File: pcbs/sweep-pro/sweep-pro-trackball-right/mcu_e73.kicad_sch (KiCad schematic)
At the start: 33 parts, among them J11 Conn_01x04_Female, J12 USB-C USB 2.0 MC-372, Q1 AO3407, Q2 AO3407, U1 E73-2G4M08S1C, U2 SRV05-4, U3 XC6220B331MR-G, U4 MAX17048, U5 TP4054, X1 32.768 kHz

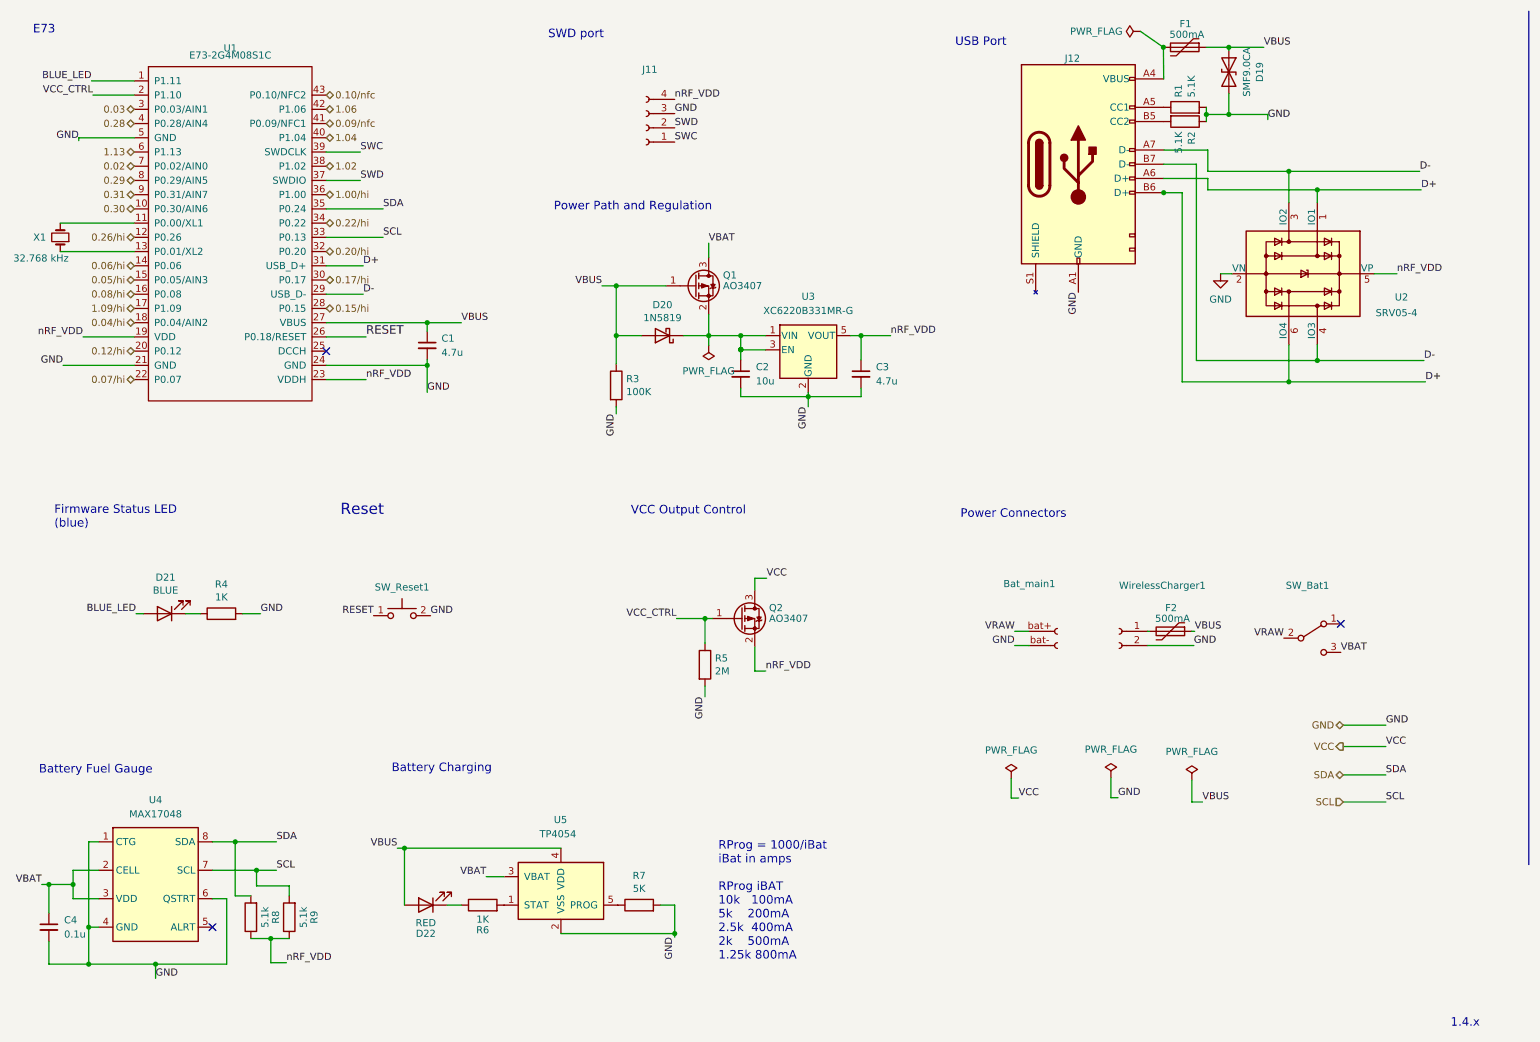
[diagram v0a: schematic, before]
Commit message: init version with integrated trackball in thumb position
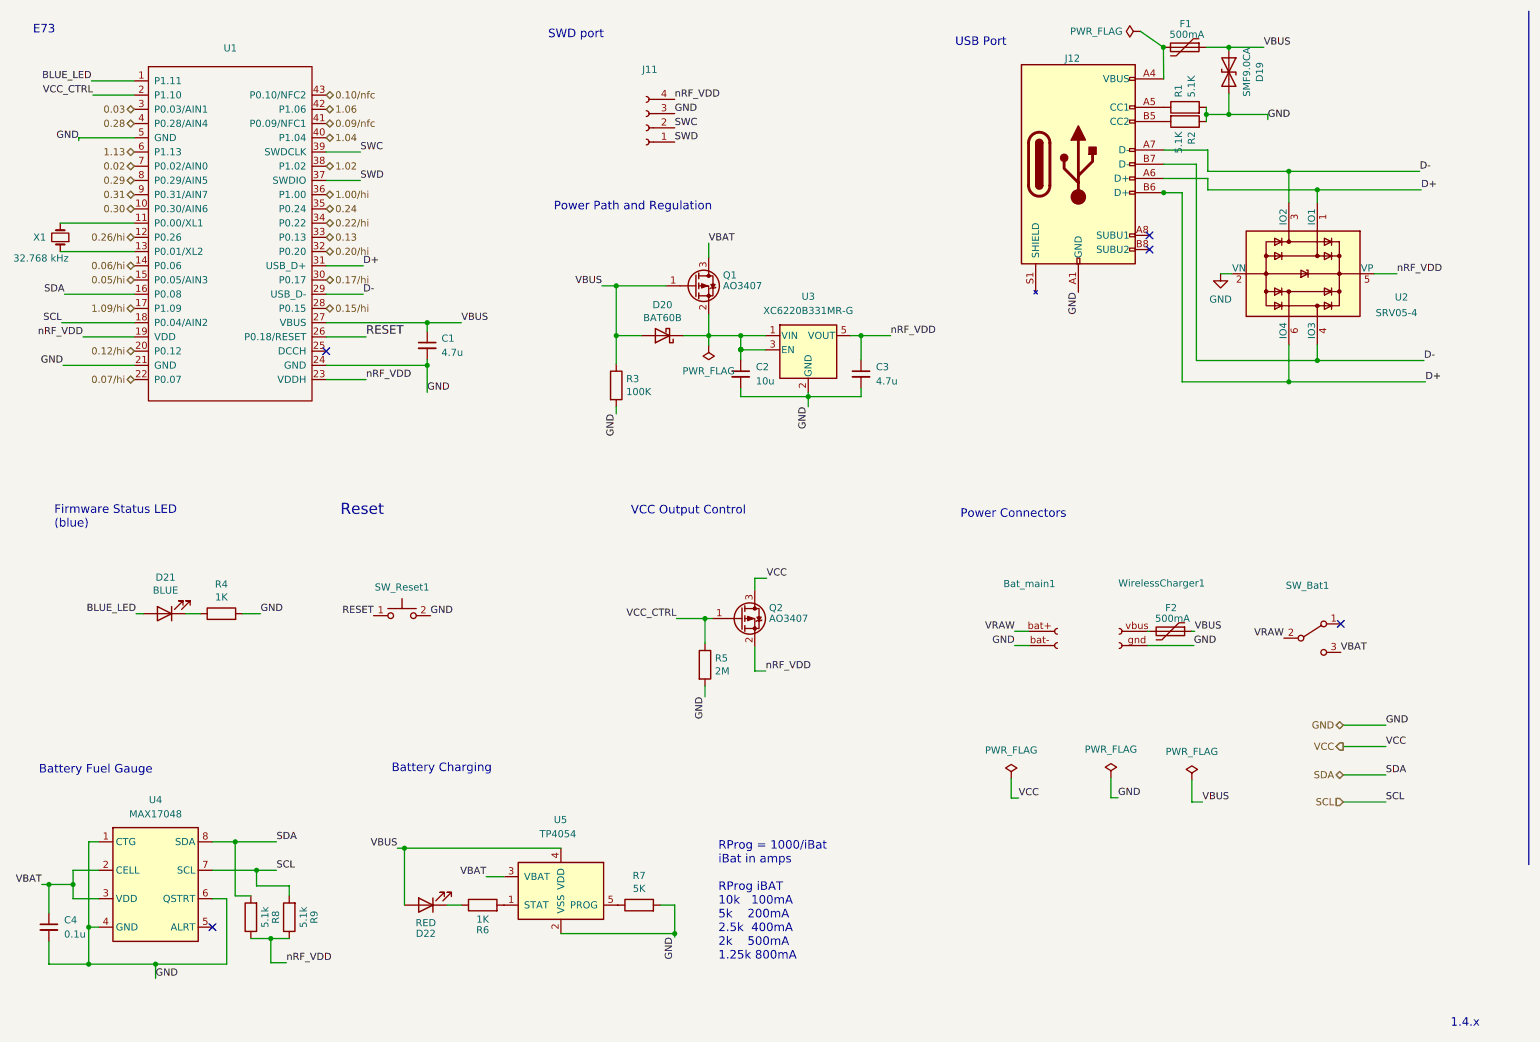
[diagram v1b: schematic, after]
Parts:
- D19: footprint Diode_SMD:D_SOD-123 -> Diode_SMD:D_SOD-123F
- D20: value 1N5819 -> BAT60B; footprint Diode_SMD:D_SOD-323F -> Diode_SMD:D_SOD-323
- J11: footprint (none) -> Connector_PinHeader_2.54mm:PinHeader_1x04_P2.54mm_Vertical
- U1: footprint nrfmicro:E73-2G4M08S1C-52840 -> mylib:E73-2G4M08S1C-52840
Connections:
- net 0.04/hi is gone; now on net SCL: U1.18 (P0.04/AIN2)
- net 0.08/hi is gone; now on net SDA: U1.16 (P0.08)
- net GND: now also WirelessCharger1.gnd; no longer WirelessCharger1.2 (Pin_2)
- net SCL: no longer U1.33 (P0.13)
- net SDA: no longer U1.35 (P0.24)
- net SWC: now also J11.2 (Pin_2); no longer J11.1 (Pin_1)
- net SWD: now also J11.1 (Pin_1); no longer J11.2 (Pin_2)
- net at F2.2: now also WirelessCharger1.vbus; no longer WirelessCharger1.1 (Pin_1)
- new net 0.13: U1.33 (P0.13)
- new net 0.24: U1.35 (P0.24)
- no-connect marks 3 -> 5
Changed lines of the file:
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@@
   (no_connect (at 250.7742 124.4092))
   (no_connect (at 69.596 75.692))
+  (no_connect (at 216.6112 55.0164))
+  (no_connect (at 216.6112 57.5564))
   (wire (pts (xy 191.9224 152.0444) (xy 191.9224 155.4988))
     (stroke (width 0) (type default) (color 0 0 0 0))
@@
     (stroke (width 0) (type default) (color 0 0 0 0))
   )
+  (wire (pts (xy 22.86 65.532) (xy 35.306 65.532))
+    (stroke (width 0) (type default) (color 0 0 0 0))
+  )
   (wire (pts (xy 165.1 83.82) (xy 155.6766 83.82))
     (stroke (width 0) (type default) (color 0 0 0 0))
   )
+  (wire (pts (xy 22.352 70.612) (xy 35.306 70.612))
+    (stroke (width 0) (type default) (color 0 0 0 0))
+  )
   (wire (pts (xy 246.5832 46.8884) (xy 246.5832 49.1744))
     (stroke (width 0) (type default) (color 0 0 0 0))
@@
     (stroke (width 0) (type default) (color 0 0 0 0))
   )
-  (wire (pts (xy 69.596 55.372) (xy 79.756 55.372))
-    (stroke (width 0) (type default) (color 0 0 0 0))
-  )
   (wire (pts (xy 56.134 172.974) (xy 53.34 172.974))
     (stroke (width 0) (type default) (color 0 0 0 0))
@@
   )
   (wire (pts (xy 87.63 78.232) (xy 87.63 77.216))
-    (stroke (width 0) (type default) (color 0 0 0 0))
-  )
-  (wire (pts (xy 69.596 50.292) (xy 79.756 50.292))
     (stroke (width 0) (type default) (color 0 0 0 0))
   )
@@
     (effects (font (size 1.27 1.27)) (justify left bottom))
   )
-  (label "GND" (at 88.2142 122.936 0)
-    (effects (font (size 1.27 1.27)) (justify left bottom))
+  (label "RESET" (at 78.0542 122.936 180)
+    (effects (font (size 1.27 1.27)) (justify right bottom))
   )
   (label "GND" (at 39.116 187.706 0)
@@
     (effects (font (size 1.27 1.27)) (justify right bottom))
   )
-  (label "SCL" (at 79.756 55.372 0)
-    (effects (font (size 1.27 1.27)) (justify left bottom))
-  )
   (label "GND" (at 87.63 83.058 0)
     (effects (font (size 1.27 1.27)) (justify left bottom))
+  )
+  (label "SCL" (at 22.352 70.612 180)
+    (effects (font (size 1.27 1.27)) (justify right bottom))
   )
   (label "D-" (at 265.6332 77.3684 0)
@@
     (effects (font (size 1.27 1.27)) (justify right bottom))
   )
-  (label "SWD" (at 131.826 35.814 0)
+  (label "SWC" (at 131.826 35.814 0)
     (effects (font (size 1.27 1.27)) (justify left bottom))
   )
@@
     (effects (font (size 1.27 1.27)) (justify left bottom))
   )
-  (label "RESET" (at 78.0542 122.936 180)
-    (effects (font (size 1.27 1.27)) (justify right bottom))
+  (label "SDA" (at 22.86 65.532 180)
+    (effects (font (size 1.27 1.27)) (justify right bottom))
+  )
+  (label "GND" (at 88.2142 122.936 0)
+    (effects (font (size 1.27 1.27)) (justify left bottom))
   )
   (label "nRF_VDD" (at 170.3832 72.9234 0)
@@
     (effects (font (size 1.27 1.27)) (justify left bottom))
   )
-  (label "SDA" (at 79.756 50.292 0)
-    (effects (font (size 1.27 1.27)) (justify left bottom))
-  )
   (label "nRF_VDD" (at 260.8072 61.8744 0)
     (effects (font (size 1.27 1.27)) (justify left bottom))
@@
     (effects (font (size 1.27 1.27)) (justify left bottom))
   )
-  (label "SWC" (at 131.826 38.354 0)
+  (label "SWD" (at 131.826 38.354 0)
     (effects (font (size 1.27 1.27)) (justify left bottom))
   )
@@
     (effects (font (size 1.27 1.27)) (justify right))
   )
+  (hierarchical_label "0.13" (shape bidirectional) (at 69.596 55.372 0)
+    (effects (font (size 1.27 1.27)) (justify left))
+  )
   (hierarchical_label "0.02" (shape bidirectional) (at 35.306 42.672 180)
     (effects (font (size 1.27 1.27)) (justify right))
@@
     (effects (font (size 1.27 1.27)) (justify left))
   )
-  (hierarchical_label "0.04{slash}hi" (shape bidirectional) (at 35.306 70.612 180)
-    (effects (font (size 1.27 1.27)) (justify right))
-  )
   (hierarchical_label "0.10{slash}nfc" (shape bidirectional) (at 69.596 29.972 0)
     (effects (font (size 1.27 1.27)) (justify left))
@@
     (effects (font (size 1.27 1.27)) (justify right))
   )
+  (hierarchical_label "0.24" (shape bidirectional) (at 69.596 50.292 0)
+    (effects (font (size 1.27 1.27)) (justify left))
+  )
   (hierarchical_label "0.03" (shape bidirectional) (at 35.306 32.512 180)
     (effects (font (size 1.27 1.27)) (justify right))
@@
   )
   (hierarchical_label "0.29" (shape bidirectional) (at 35.306 45.212 180)
-    (effects (font (size 1.27 1.27)) (justify right))
-  )
-  (hierarchical_label "0.08{slash}hi" (shape bidirectional) (at 35.306 65.532 180)
     (effects (font (size 1.27 1.27)) (justify right))
   )
@@
     (pin "A6")
     (pin "A7")
+    (pin "A8")
     (pin "B5")
     (pin "B6")
     (pin "B7")
+    (pin "B8")
     (pin "S1")
   )
@@
       (effects (font (size 0 0)))
     )
-    (property "Value" "E73-2G4M08S1C" (id 1) (at 52.451 22.86 0))
-    (property "Footprint" "nrfmicro:E73-2G4M08S1C-52840" (id 2) (at 53.086 55.372 0)
+    (property "Value" "E73-2G4M08S1C" (id 1) (at 52.451 22.86 0)
+      (effects (font (size 1.27 1.27)) hide)
+    )
+    (property "Footprint" "mylib:E73-2G4M08S1C-52840" (id 2) (at 53.086 55.372 0)
       (effects (font (size 1.27 1.27)) hide)
     )
@@
     (property "Reference" "D19" (id 0) (at 236.2962 25.8572 0))
     (property "Value" "SMF9.0CA" (id 1) (at 233.9848 25.8572 0))
-    (property "Footprint" "Diode_SMD:D_SOD-123" (id 2) (at 230.7844 25.8572 0)
+    (property "Footprint" "Diode_SMD:D_SOD-123F" (id 2) (at 230.7844 25.8572 0)
       (effects (font (size 1.27 1.27)) hide)
     )
@@
   (symbol (lib_id "Connector:Conn_01x02_Female") (at 211.201 125.73 0) (mirror y) (unit 1)
     (in_bom no) (on_board yes)
-    (property "Reference" "WirelessCharger1" (id 0) (at 226.6442 117.5512 0)
+    (property "Reference" "WirelessCharger1" (id 0) (at 226.5172 117.1448 0)
       (effects (font (size 1.27 1.27)) (justify left))
     )
@@
       (effects (font (size 1.27 1.27)) hide)
     )
-    (pin "1")
-    (pin "2")
+    (pin "gnd")
+    (pin "vbus")
   )
   (symbol (lib_id "Device:LED") (at 40.7162 122.5804 180) (unit 1)
@@
       (effects (font (size 1.27 1.27)) hide)
     )
-    (property "Footprint" "" (id 2) (at 126.746 35.814 0)
+    (property "Footprint" "Connector_PinHeader_2.54mm:PinHeader_1x04_P2.54mm_Vertical" (id 2) (at 126.746 35.814 0)
       (effects (font (size 1.27 1.27)) hide)
     )
@@
     (in_bom yes) (on_board yes)
     (property "Reference" "D20" (id 0) (at 129.6416 67.437 0))
-    (property "Value" "1N5819" (id 1) (at 129.6416 69.7484 0))
-    (property "Footprint" "Diode_SMD:D_SOD-323F" (id 2) (at 129.6416 68.4784 0)
-      (effects (font (size 1.27 1.27)) hide)
-    )
+    (property "Value" "BAT60B" (id 1) (at 129.6416 69.7484 0))
+    (property "Footprint" "Diode_SMD:D_SOD-323" (id 2) (at 129.6416 68.4784 0)
+      (effects (font (size 1.27 1.27)) hide)
+    )
